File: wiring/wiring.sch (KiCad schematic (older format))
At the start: 17 parts, among them J1 D, J10 H, J11 DEFGH, J2 M, J3 E, J4 C, J5 F, J6 A, J7 B, J8 S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

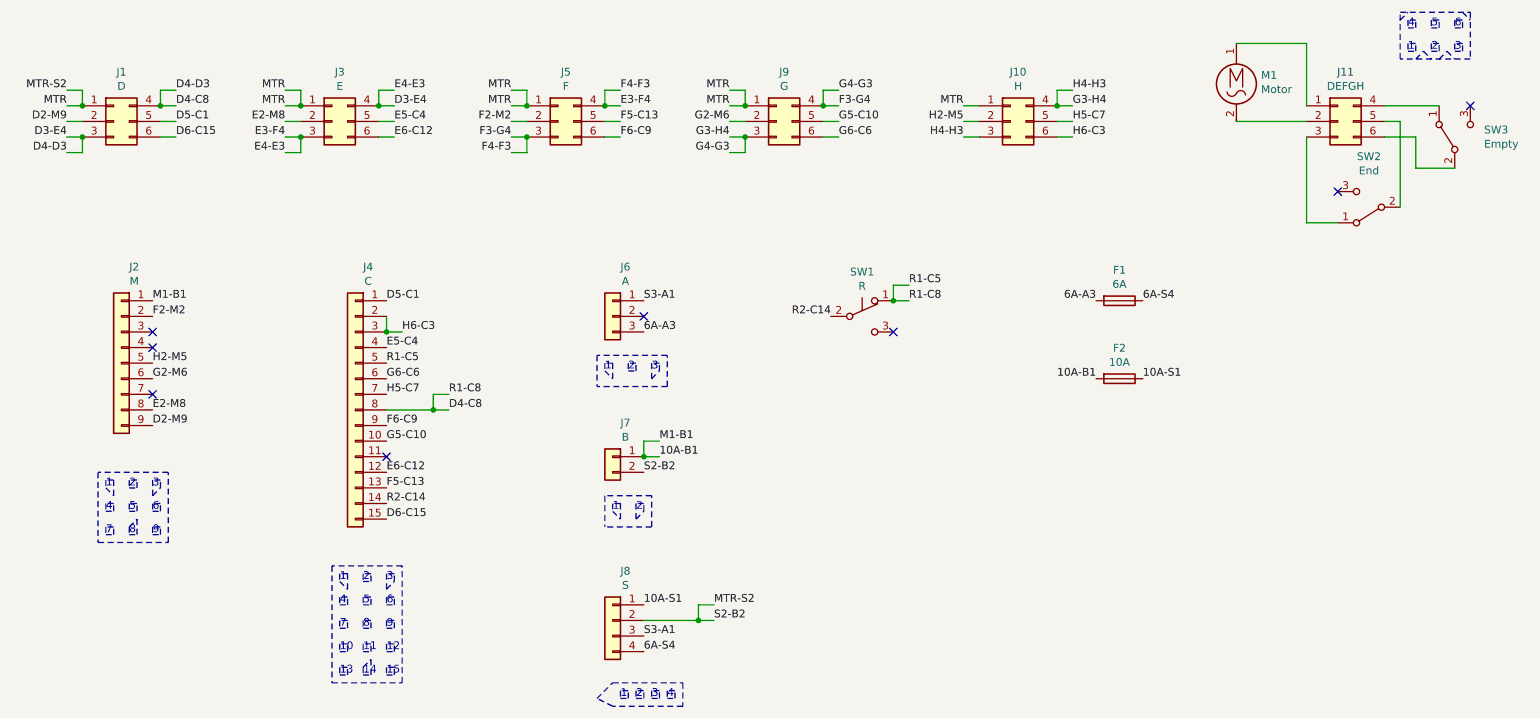
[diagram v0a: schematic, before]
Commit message: wiring: Added some descriptions
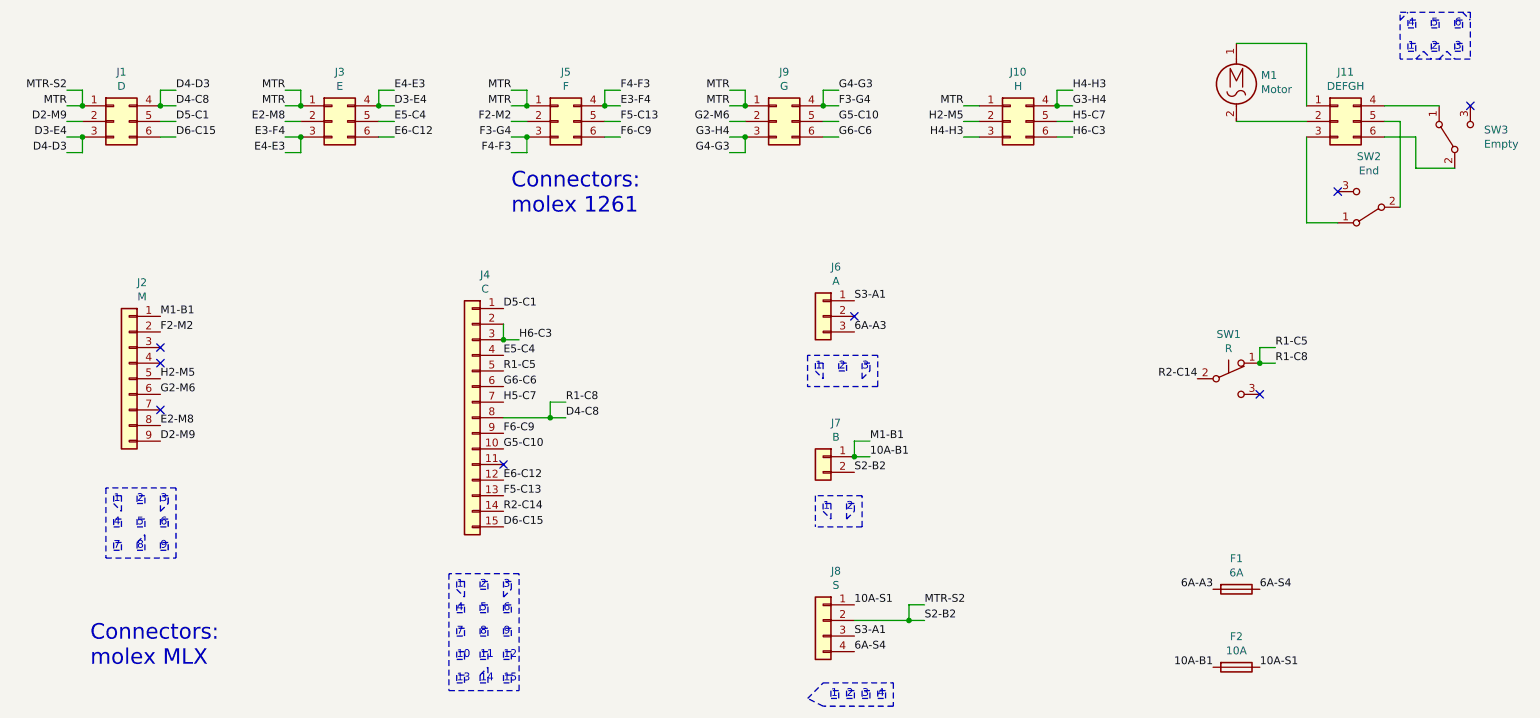
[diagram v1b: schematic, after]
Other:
- note added: "Connectors:\nmolex 1261"
- note added: "Connectors:\nmolex MLX"
- moved on the sheet: F1, F2, J2, J4, J6, J7, J8, SW1
